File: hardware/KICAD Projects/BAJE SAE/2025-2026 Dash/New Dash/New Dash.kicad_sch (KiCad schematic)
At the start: 5 parts, among them J1 CAN to outer connector, J999 Conn_01x06, U1 XIAO-ESP32-S3-SMD

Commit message: Pasted in Connectors
Added Servo Connectors
Button connectors
socket
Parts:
- added J1-1, J1-2, J11-1, J11-2: Conn_01x05, Connector_PinHeader_2.54mm:PinHeader_1x05_P2.54mm_Vertical, symbol Connector_Generic:Conn_01x05
- added J10: Servo 1 (RPM), Connector_PinHeader_2.54mm:PinHeader_1x03_P2.54mm_Vertical, symbol Connector_Generic:Conn_01x03
- added J2: Servo 2 (Speed), Connector_PinHeader_2.54mm:PinHeader_1x03_P2.54mm_Vertical, symbol Connector_Generic:Conn_01x03
- added J4: Button 1, Connector_PinHeader_2.54mm:PinHeader_1x02_P2.54mm_Vertical, symbol Connector_Generic:Conn_01x02
- added J5: 14 Segment (1), Connector_PinHeader_2.54mm:PinHeader_1x04_P2.54mm_Vertical, symbol Connector_Generic:Conn_01x04
- added J6: 14 Segment (2), Connector_PinHeader_2.54mm:PinHeader_1x04_P2.54mm_Vertical, symbol Connector_Generic:Conn_01x04
- added J7: 14 Segment (3), Connector_PinHeader_2.54mm:PinHeader_1x04_P2.54mm_Vertical, symbol Connector_Generic:Conn_01x04
- added J8: 14 Segment (4), Connector_PinHeader_2.54mm:PinHeader_1x04_P2.54mm_Vertical, symbol Connector_Generic:Conn_01x04
- added J9: Button 2, Connector_PinHeader_2.54mm:PinHeader_1x02_P2.54mm_Vertical, symbol Connector_Generic:Conn_01x02
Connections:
- net +5v: now also J10.2 (Pin_2), J2.2 (Pin_2)
- net 3v3 ground: now also J5.4 (Pin_4), J6.4 (Pin_4), J7.4 (Pin_4), J8.4 (Pin_4)
- net A0: now also J11-1.1 (Pin_1)
- net A1: now also J11-1.2 (Pin_2)
- net A10: now also J1-1.3 (Pin_3)
- net A11: now also J1-1.4 (Pin_4)
- net A12: now also J1-1.5 (Pin_5)
- net A13: now also J1-2.1 (Pin_1)
- net A14: now also J1-2.2 (Pin_2)
- net A15: now also J1-2.3 (Pin_3)
- net A2: now also J11-1.3 (Pin_3)
- net A3: now also J11-1.4 (Pin_4)
- net A4: now also J11-1.5 (Pin_5)
- net A5: now also J11-2.1 (Pin_1)
- net A6: now also J11-2.2 (Pin_2)
- net A7: now also J11-2.3 (Pin_3)
- net A8: now also J1-1.1 (Pin_1)
- net A9: now also J1-1.2 (Pin_2)
- net C0: now also J1-2.4 (Pin_4), J11-2.4 (Pin_4)
- net C1: now also J1-2.5 (Pin_5), J11-2.5 (Pin_5)
- net GND: now also J10.1 (Pin_1), J2.1 (Pin_1), J4.2 (Pin_2), J9.2 (Pin_2)
- net Regulated 3v3: now also J5.3 (Pin_3), J6.3 (Pin_3), J7.3 (Pin_3), J8.3 (Pin_3)
- net SCL: now also J5.1 (Pin_1), J6.1 (Pin_1), J7.1 (Pin_1), J8.1 (Pin_1)
- net SDA: now also J5.2 (Pin_2), J6.2 (Pin_2), J7.2 (Pin_2), J8.2 (Pin_2)
- new net IO12 Button 1: J4.1 (Pin_1)
- new net IO14 Button 2: J9.1 (Pin_1)
- new net IO32 Speed: J2.3 (Pin_3)
- new net IO33 RPM: J10.3 (Pin_3)
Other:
- note added: "14 Segments"
- note added: "Buttons"
- note added: "ESP-32 Socketed with ESS-119-T-03"
- note added: "Servos"
- note added: "Socket"

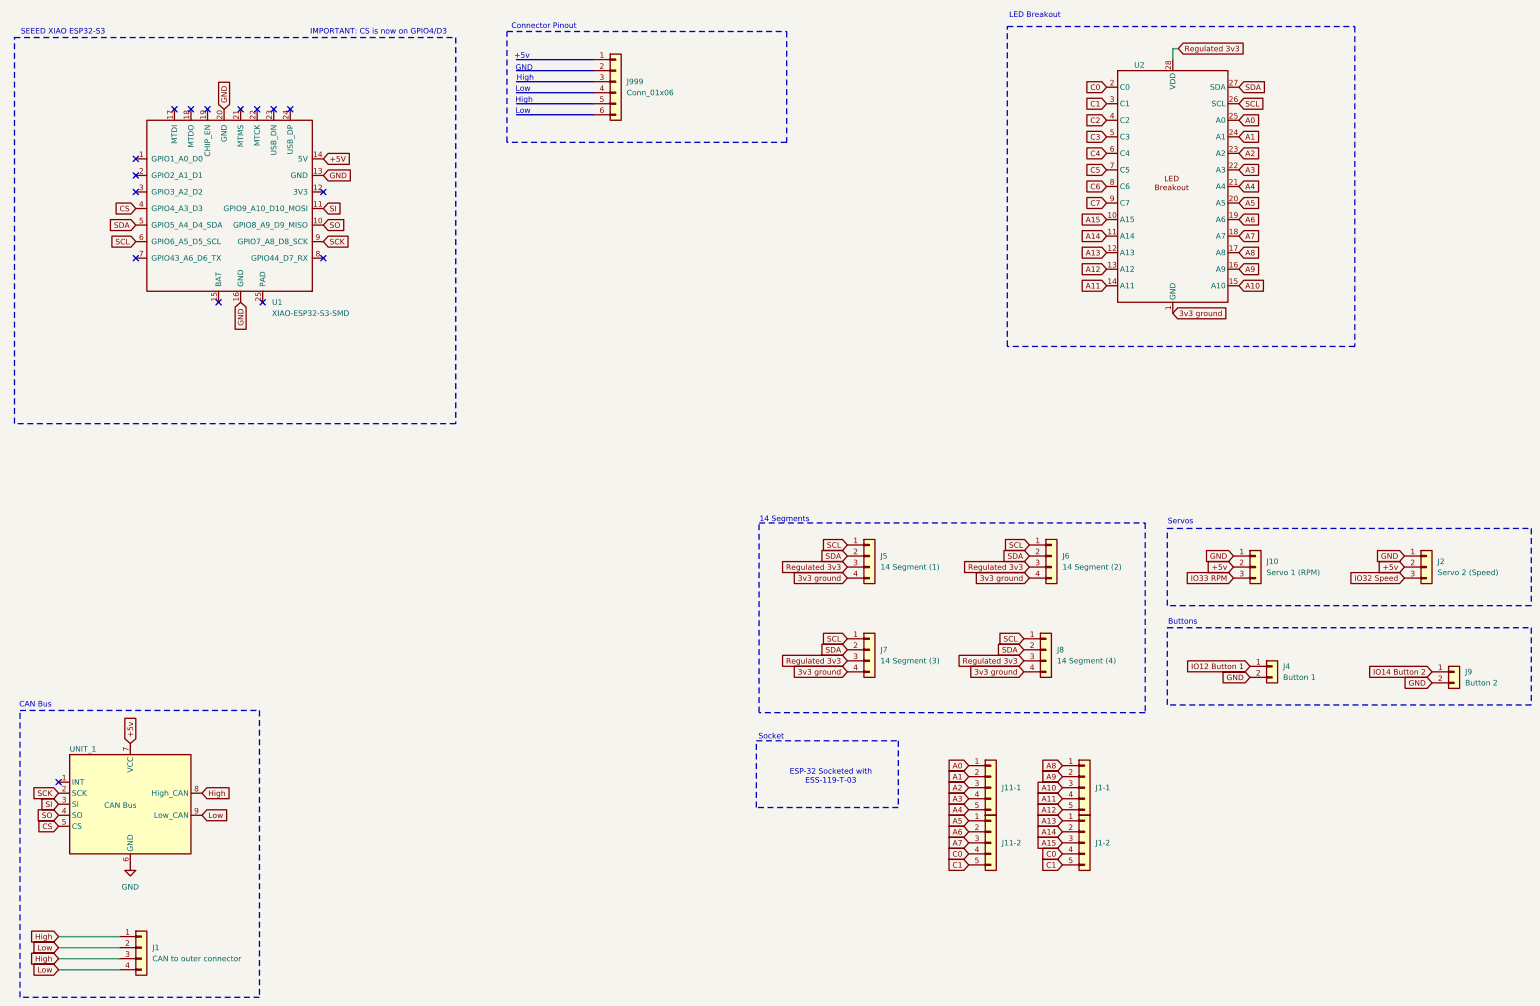
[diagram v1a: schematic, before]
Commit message: Pasted in the rest of the components
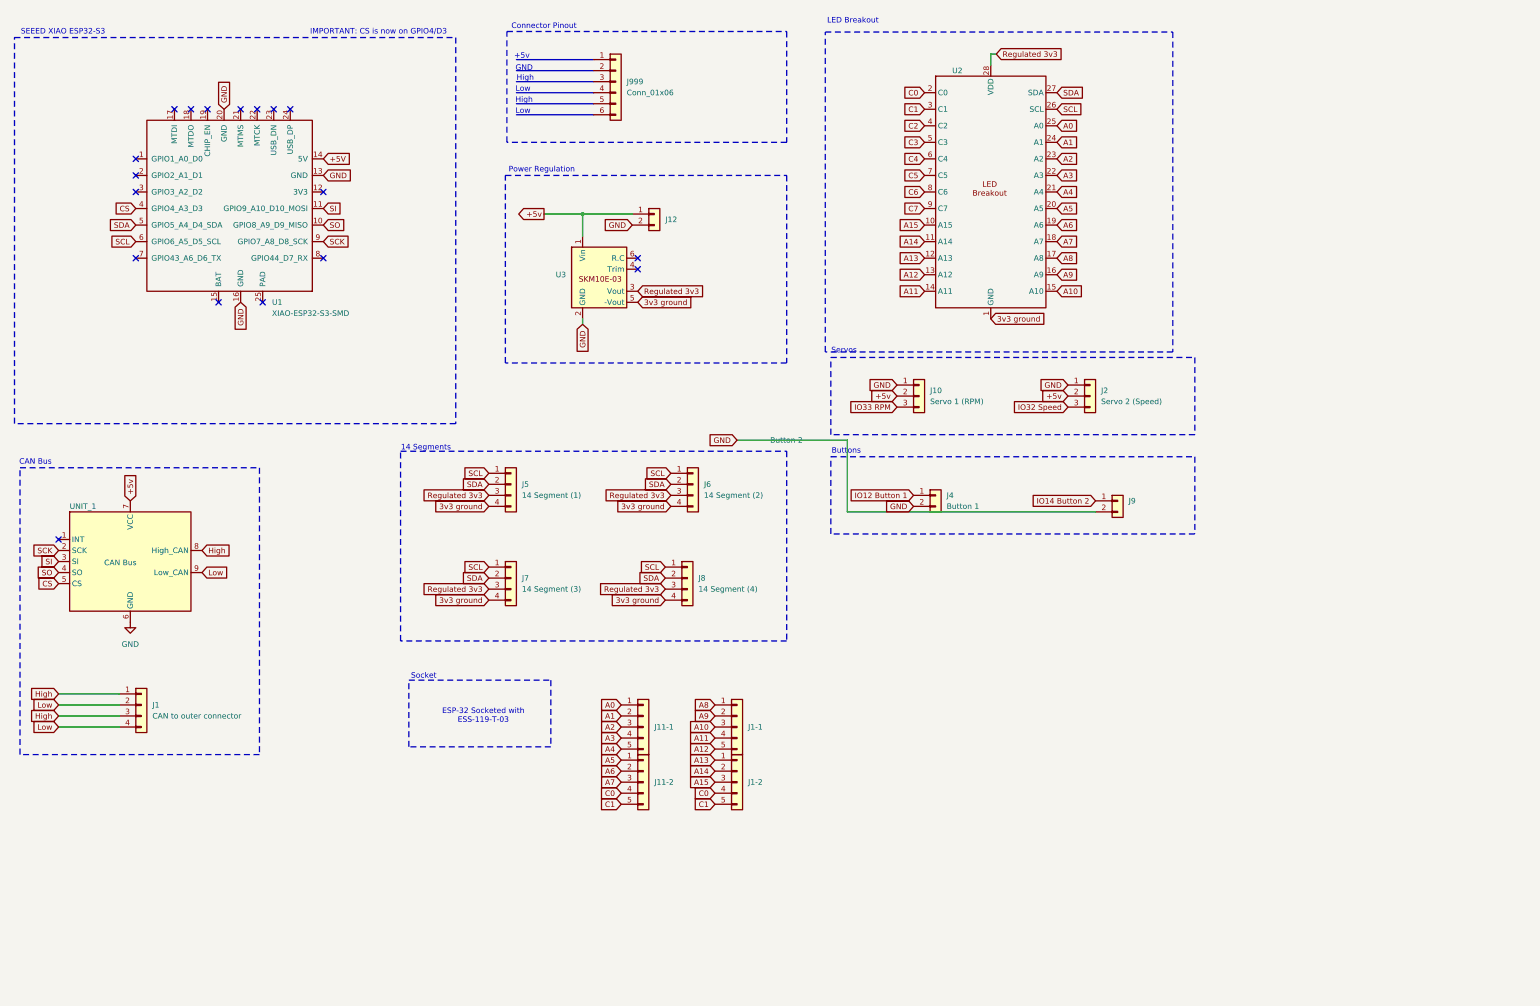
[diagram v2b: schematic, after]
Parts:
- added J12: Conn_01x02, Connector_Wire:SolderWire-0.75sqmm_1x02_P4.8mm_D1.25mm_OD2.3mm, symbol Connector_Generic:Conn_01x02
- added U3: ~, 0_Baja_Final:SKM10E-03, symbol 0_Baja_Final:SKM10E-03
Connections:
- net +5v: now also J12.1 (Pin_1), U3.1 (Vin)
- net 3v3 ground: now also U3.5 (-Vout)
- net GND: now also J12.2 (Pin_2), U3.2 (GND)
- net Regulated 3v3: now also U3.3 (Vout)
- no-connect marks 16 -> 18
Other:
- note added: "Power Regulation"
- moved on the sheet: J1, J1-1, J1-2, J10, J11-1, J11-2, J2, J4, J5, J6, J7, J8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
